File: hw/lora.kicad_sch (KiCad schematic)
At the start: 11 parts, among them J2 WM1302_SPI_EU868, U4 ATECC608B-SSHDA, U5 SN74LVC1G17DBVR

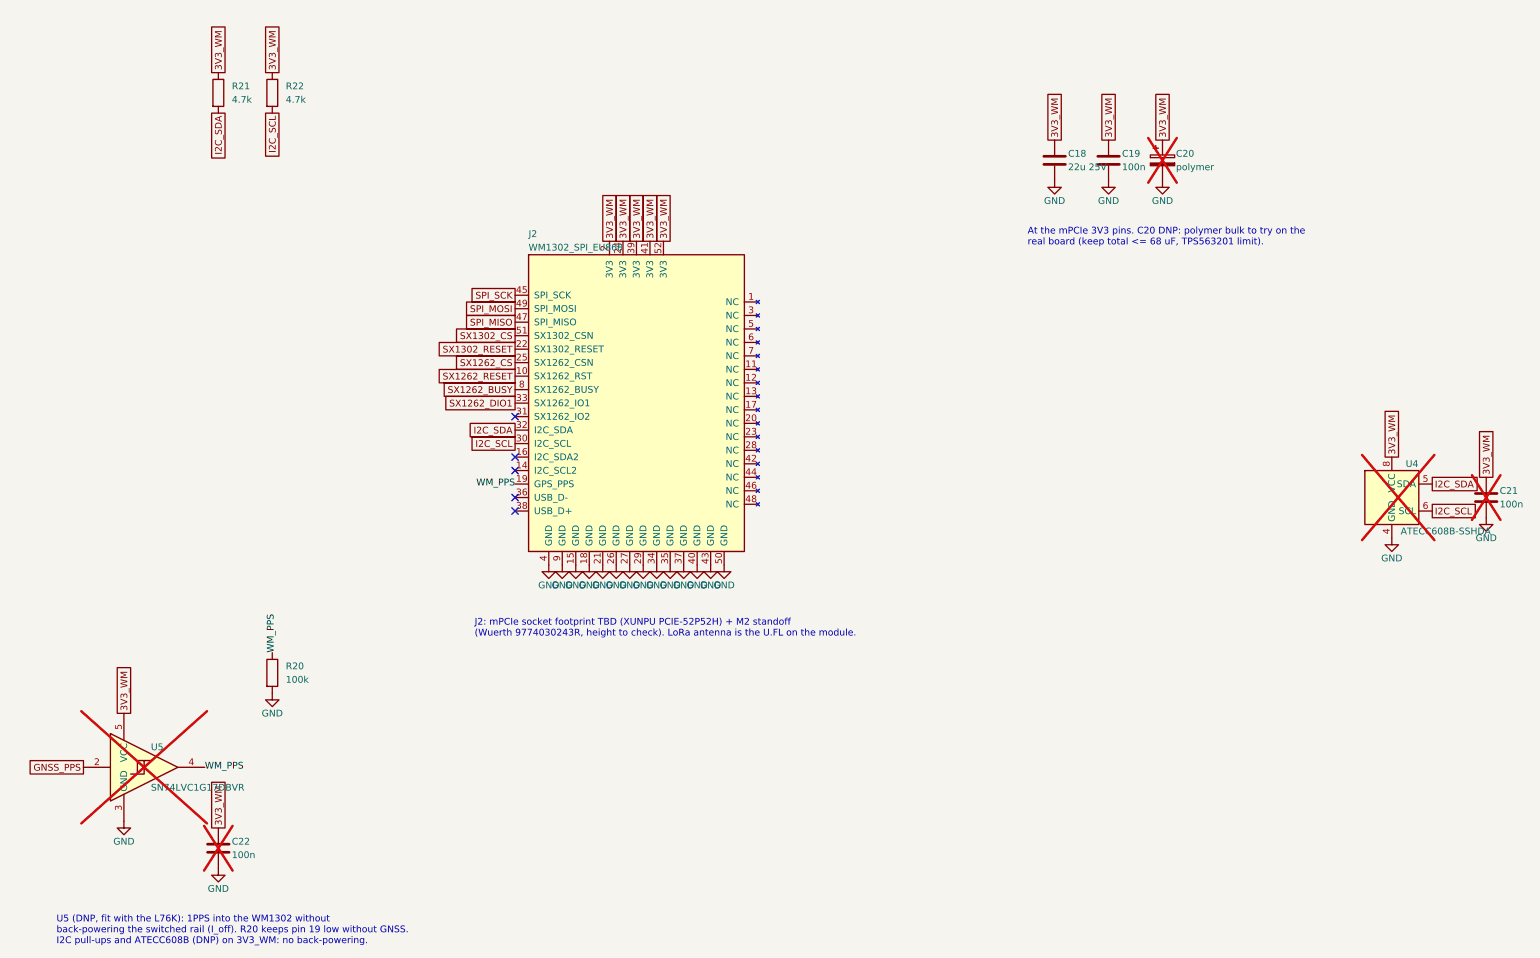
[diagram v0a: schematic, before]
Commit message: hw: draw schematic with wires instead of net labels
Connections inside a sheet are now wires; global labels remain only for
nets that cross sheets, GND stays on power symbols. Pico pins 9-20 are
fanned out so the 33R series resistors fit in one column, and the
SX1302_RESET pull-down moves to the LoRa sheet. Netlist unchanged, ERC
clean. Project file now carries KiCad's default settings.

Co-Authored-By: Claude Opus 5.5 <noreply@anthropic.com>
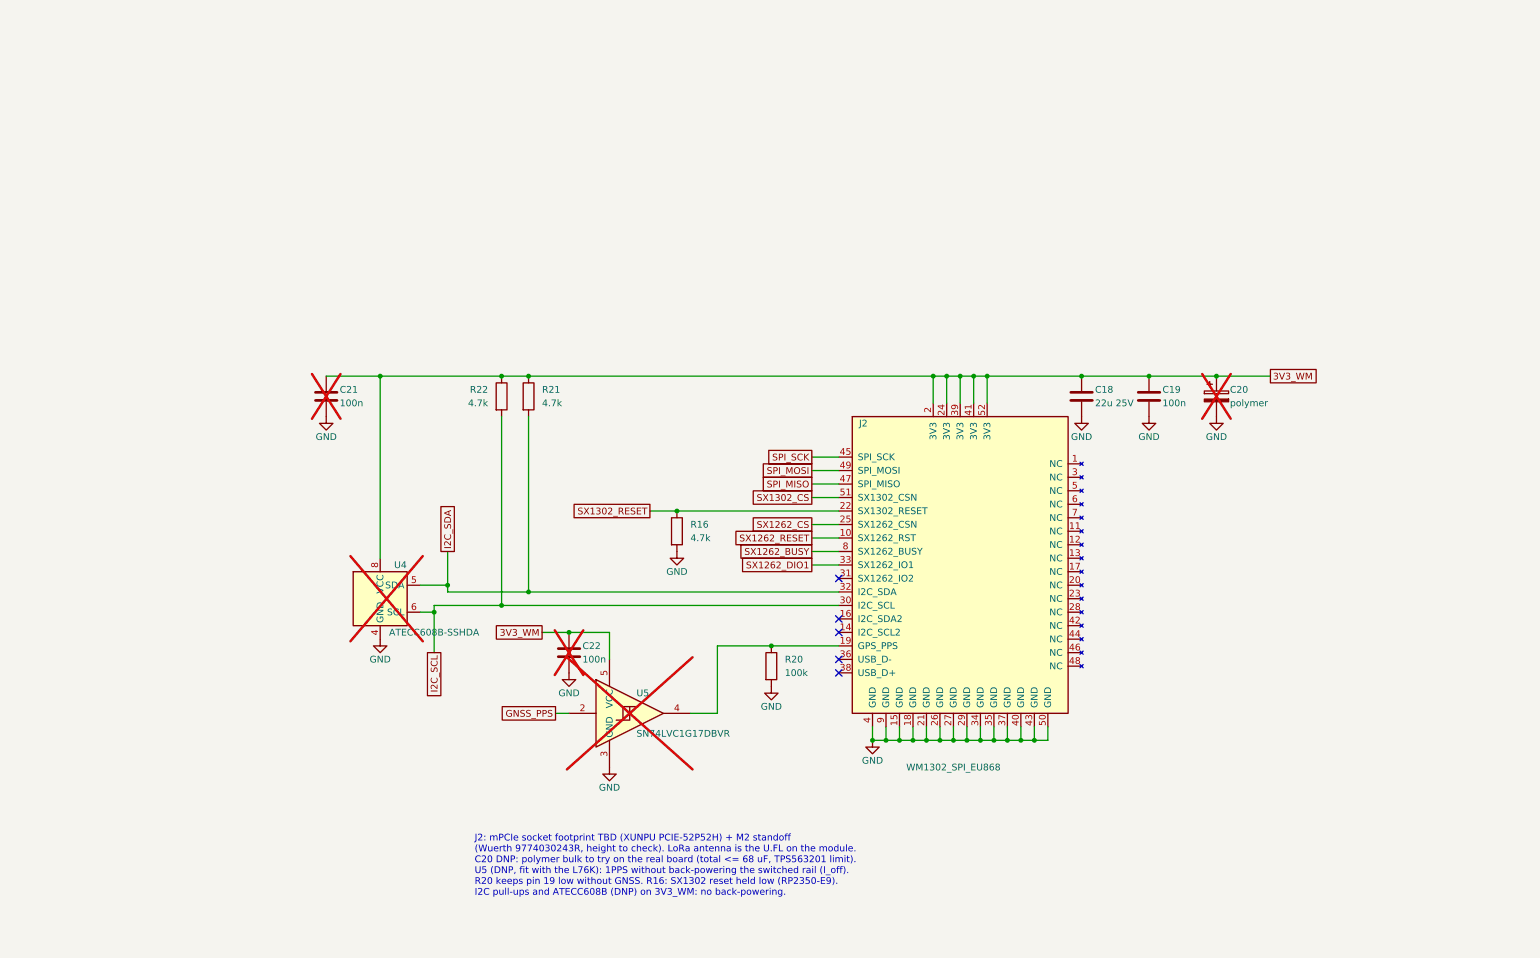
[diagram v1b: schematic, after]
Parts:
- added R16: 4.7k, Resistor_SMD:R_0603_1608Metric, symbol Device:R
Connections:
- net GND: now also R16.2
- net SX1302_RESET: now also R16.1
- net WM_PPS: no longer names the net of J2.19 (GPS_PPS), R20.1, U5.4
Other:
- note added: "J2: mPCIe socket footprint TBD (XUNPU PCIE-52P52H) + M2 standoff (Wuerth 9774030243R, height to check). LoRa antenna is the U.FL on the module. C20 DNP: polymer bulk to try on the real board (total <= 68 uF, TPS563201 limit). U5 (DNP, fit with the L76K): 1PPS without back-powering the switched rail (I_off). R20 keeps pin 19 low without GNSS. R16: SX1302 reset held low (RP2350-E9). I2C pull-ups an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"
- note removed: "At the mPCIe 3V3 pins. C20 DNP: polymer bulk to try on the real board (keep total <= 68 uF, TPS563201 limit)."
- note removed: "J2: mPCIe socket footprint TBD (XUNPU PCIE-52P52H) + M2 standoff (Wuerth 9774030243R, height to check). LoRa antenna is the U.FL on the module."
- note removed: "U5 (DNP, fit with the L76K): 1PPS into the WM1302 without back-powering the switched rail (I_off). R20 keeps pin 19 low without GNSS. I2C pull-ups and ATECC608B (DNP) on 3V3_WM: no back-powering."
- moved on the sheet: C18, C19, C20, C21, C22, J2, R20, R21, R22, U4, U5

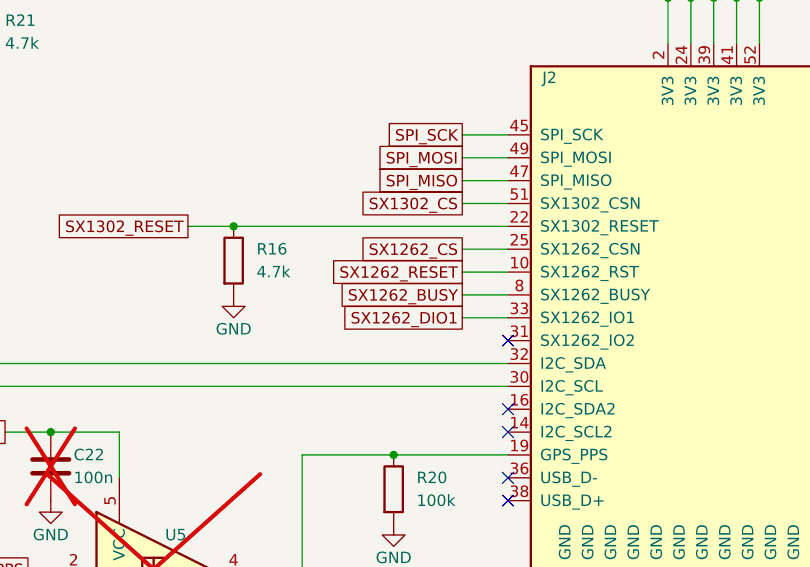
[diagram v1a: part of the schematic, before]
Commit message: sketch, hw: drop SX1262 (LBT/spectral scan), use WM1302 variant without it
LBT is not required in EU868 (ETSI duty cycle applies), so the cheaper
WM1302 SPI variant without the SX1262 is enough. Remove the SX1262 nets
and the CS series resistor R12, mark GP6-GP9 and mPCIe pins 8/10/25/33
as no-connect.

Co-Authored-By: Claude Opus 5.5 <noreply@anthropic.com>
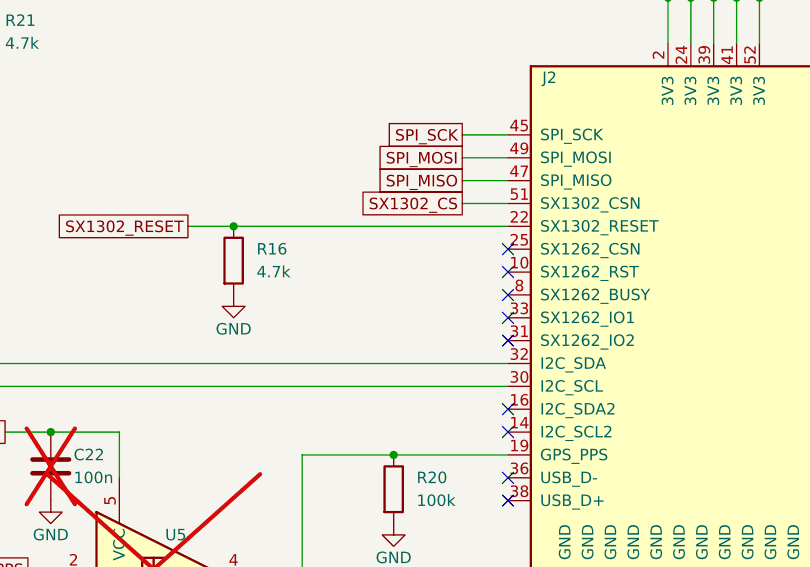
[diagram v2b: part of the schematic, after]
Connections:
- net SX1262_BUSY: no longer names the net of J2.8 (SX1262_BUSY)
- net SX1262_CS: no longer names the net of J2.25 (SX1262_CSN)
- net SX1262_DIO1: no longer names the net of J2.33 (SX1262_IO1)
- net SX1262_RESET: no longer names the net of J2.10 (SX1262_RST)
- no-connect marks 5 -> 9
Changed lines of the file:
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@@
-		)
-	)
-	(global_label "SX1262_CS"
-		(shape passive)
-		(at 187.96 132.08 180)
-		(fields_autoplaced yes)
-		(effects
-			(font
-				(size 1.27 1.27)
-			)
-			(justify right)
-		)
-		(property "Intersheetrefs" "${INTERSHEET_REFS}"
-			(at 187.96 132.08 180)
-			(effects
-				(font
-					(size 1.27 1.27)
-				)
-				(justify right)
-				(hide yes)
-			)
-		)
-	)
-	(global_label "SX1262_RESET"
-		(shape passive)
-		(at 187.96 134.62 180)
-		(fields_autoplaced yes)
-		(effects
-			(font
-				(size 1.27 1.27)
-			)
-			(justify right)
-		)
-		(property "Intersheetrefs" "${INTERSHEET_REFS}"
-			(at 187.96 134.62 180)
-			(effects
-				(font
-					(size 1.27 1.27)
-				)
-				(justify right)
-				(hide yes)
-			)
-		)
-	)
-	(global_label "SX1262_BUSY"
-		(shape passive)
-		(at 187.96 137.16 180)
-		(fields_autoplaced yes)
-		(effects
-			(font
-				(size 1.27 1.27)
-			)
-			(justify right)
-		)
-		(property "Intersheetrefs" "${INTERSHEET_REFS}"
-			(at 187.96 137.16 180)
-			(effects
-				(font
-					(size 1.27 1.27)
-				)
-				(justify right)
-				(hide yes)
-			)
-		)
-	)
-	(global_label "SX1262_DIO1"
-		(shape passive)
-		(at 187.96 139.7 180)
-		(fields_autoplaced yes)
-		(effects
-			(font
-				(size 1.27 1.27)
-			)
-			(justify right)
-		)
-		(property "Intersheetrefs" "${INTERSHEET_REFS}"
-			(at 187.96 139.7 180)
-			(effects
-				(font
-					(size 1.27 1.27)
-				)
-				(justify right)
-				(hide yes)
-			)
 		)
 	)
@@
 		)
 	)
+	(no_connect
+		(at 193.04 132.08)
+	)
+	(no_connect
+		(at 193.04 134.62)
+	)
+	(no_connect
+		(at 193.04 137.16)
+	)
+	(no_connect
+		(at 193.04 139.7)
+	)
 	(wire
 		(pts
@@
 		)
 		(stroke
-			(width 0)
-			(type default)
-		)
-	)
-	(wire
-		(pts
-			(xy 187.96 132.08)
-			(xy 193.04 132.08)
-		)
-		(stroke
-			(width 0)
-			(type default)
-		)
-	)
-	(wire
-		(pts
-			(xy 187.96 134.62)
-			(xy 193.04 134.62)
-		)
-		(stroke
-			(width 0)
-			(type default)
-		)
-	)
-	(wire
-		(pts
-			(xy 187.96 137.16)
-			(xy 193.04 137.16)
-		)
-		(stroke
-			(width 0)
-			(type default)
-		)
-	)
-	(wire
-		(pts
-			(xy 187.96 139.7)
-			(xy 193.04 139.7)
-		)
-		(stroke
